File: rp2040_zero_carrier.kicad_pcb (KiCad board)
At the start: 2 copper layers, 42.5 x 37.2 mm, 17 parts, among them J1 LPC, J2 SPARE, J5 EXP, J6 LCD, J7 UART

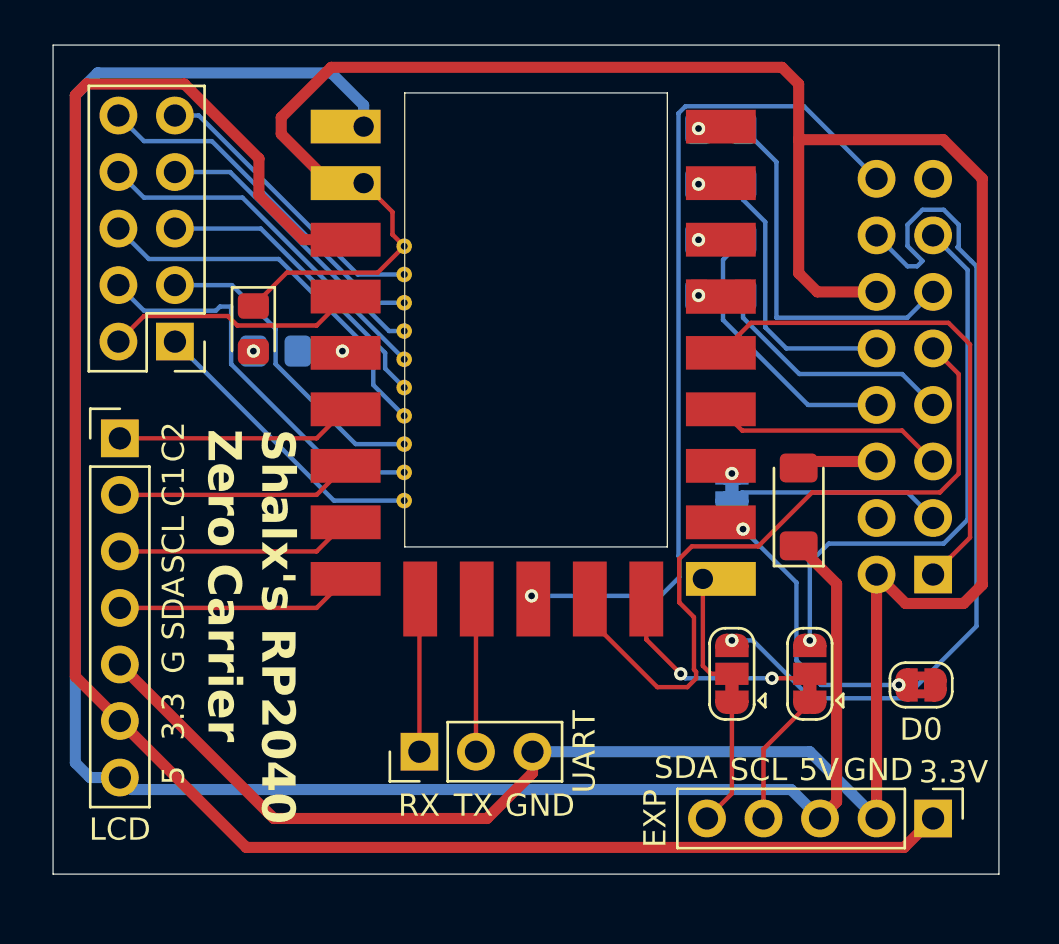
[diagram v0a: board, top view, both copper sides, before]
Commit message: Updated rp2040 zero footprint
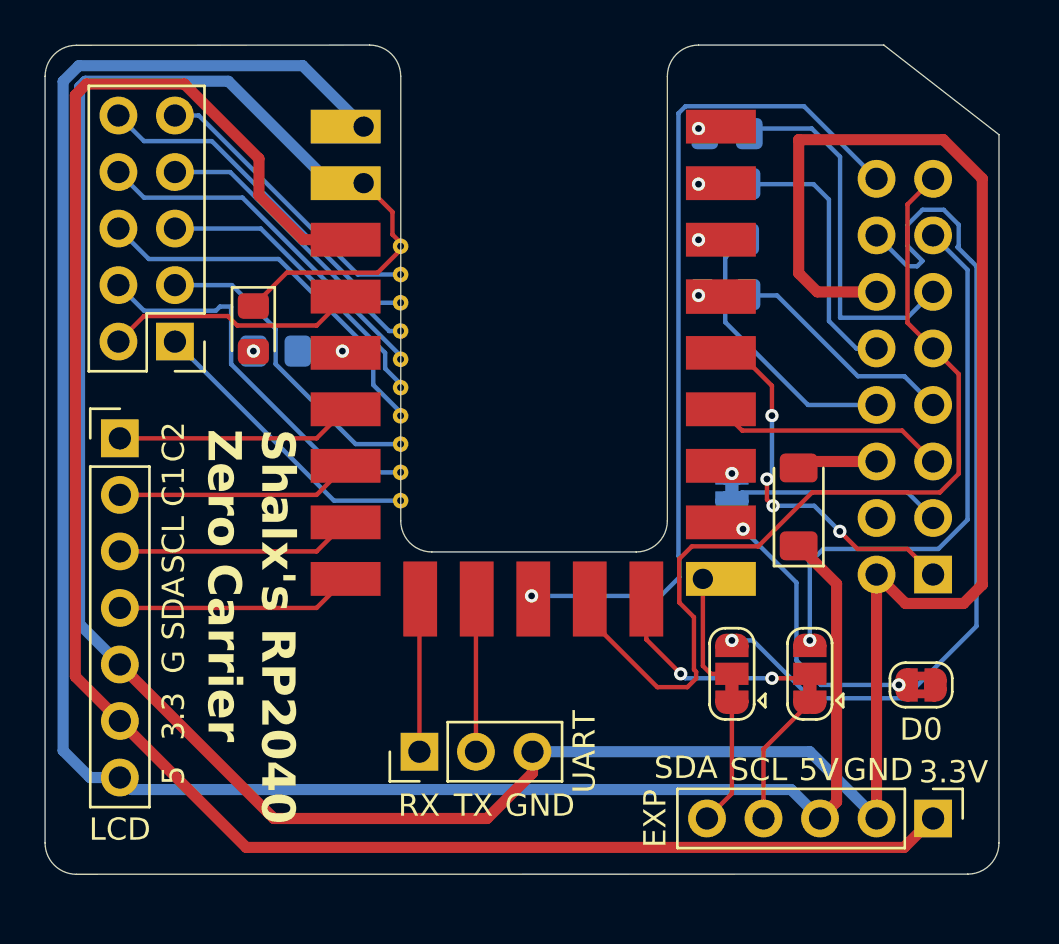
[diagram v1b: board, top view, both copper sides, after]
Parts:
- moved R1 0.36 mm to (123.8, 101.2)
- moved R4 0.18 mm to (123.7, 108.5)
- moved R2 0.18 mm to (123.7, 103.5)
- moved R3 0.12 mm to (123.6, 106.0)
- renumbered LFrame to LFrame1
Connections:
- J1 pad 15: unconnected-(J1-Pin_15-Pad15) -> /LPC 3.3
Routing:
- net GND: track 136.3 -> 146.6 mm
- net /LPC 3.3: track 33.6 -> 42.1 mm
- net /LCLK: track 23.2 -> 17.0 mm, vias 0 -> 4
- net +5V: track 92.7 -> 93.5 mm
- net Net-(J1-Pin_7): track 11.2 -> 10.6 mm
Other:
- board size 42.5 x 37.2 mm -> 42.9 x 37.3 mm
